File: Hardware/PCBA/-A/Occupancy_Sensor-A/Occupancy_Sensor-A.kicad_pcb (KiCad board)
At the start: 2 copper layers, 30 x 30 mm, 60 parts, among them J1 USB_C_Receptacle, J2 Conn_02x05_Odd_Even, Q1 2N7002, Q2 2N7002, SW1 SW_Push, SW2 SW_SPDT, U1 TPS78318DDCR, U3 TPS562200, U4 STM32WB55CGUx, U6 ECMF02-2AMX6, Y1 Crystal_GND24_Small, Y2 Crystal_GND24_Small

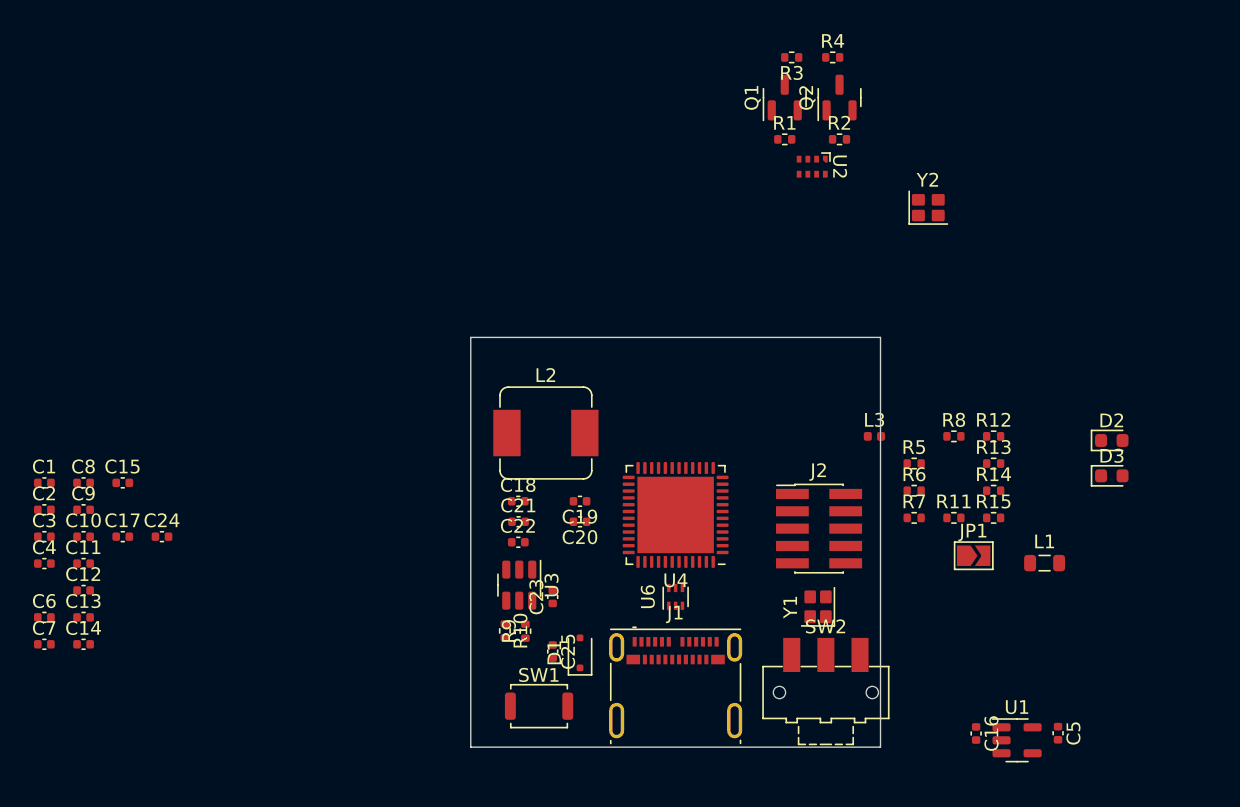
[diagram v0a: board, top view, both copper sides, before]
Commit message: General layout, regulator fixes
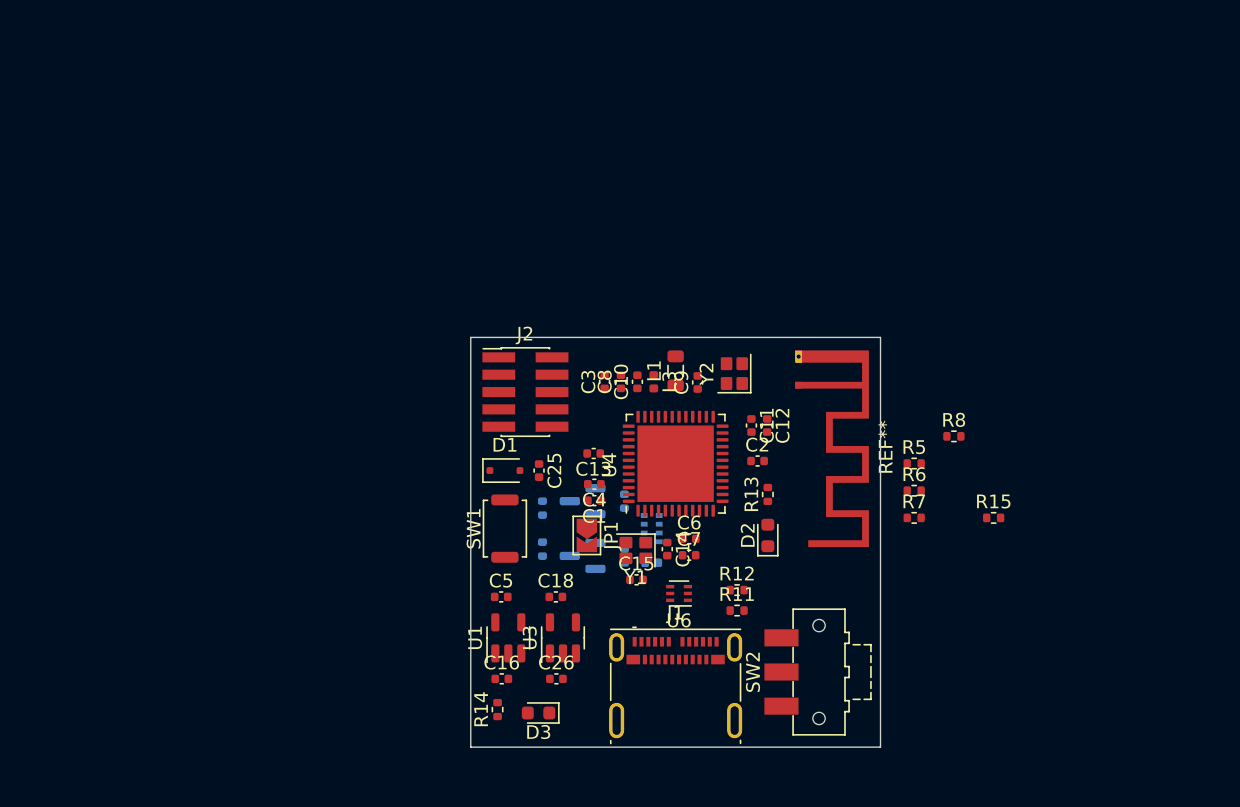
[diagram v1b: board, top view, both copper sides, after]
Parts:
- removed C19, C20: 22u, Capacitor_SMD:C_0402_1005Metric
- removed C21: 10u, Capacitor_SMD:C_0402_1005Metric
- removed C22, C23, C24: 100n, Capacitor_SMD:C_0402_1005Metric
- removed L2: 3.3u, Inductor_SMD:L_Sumida_CDMC6D28_7.25x6.5mm
- removed R10: 10K, Resistor_SMD:R_0402_1005Metric
- removed R9: 33.2K, Resistor_SMD:R_0402_1005Metric
- added C26: 1u, Capacitor_SMD:C_0402_1005Metric, F.Cu at (136.3, 125.0)
- added REF**: Texas_SWRA117D_2.4GHz_Right, RF_Antenna:Texas_SWRA117D_2.4GHz_Right, F.Cu at (154.0, 103.5)
- C17, Q1, Q2, R1, R2, R3, R4, U2: moved to B.Cu
- C18: value 10u -> 1u
- C5: value 2.2u -> 1u
- U1: value TPS78318DDCR -> TPS7A0333PDBV
- U3: value TPS562200 -> TPS7A03185PDBV; footprint Package_TO_SOT_SMD:SOT-23-6 -> Package_TO_SOT_SMD:SOT-23-5
- moved C2 52.3 mm to (151.0, 109.0)
- moved C12 51.5 mm to (151.7, 106.5), turned to -90 degrees
- moved C11 49.9 mm to (150.6, 106.5), turned to -90 degrees
- moved C7 47.7 mm to (146.0, 116.0)
- moved C6 47.6 mm to (146.0, 114.8)
- moved C9 45.9 mm to (146.6, 103.3), turned to 90 degrees
- moved D3 45.4 mm to (135.0, 127.5), turned to 180 degrees
- moved C14 43.3 mm to (144.4, 115.5), turned to -90 degrees
- moved C3 42.6 mm to (139.8, 103.2), turned to 90 degrees
- moved C10 42.1 mm to (142.2, 103.2), turned to 90 degrees
- moved C5 42.0 mm to (132.2, 119.0), turned to 0 degrees
- moved R4 41.8 mm to (135.2, 115.5), turned to -90 degrees
- moved C4 40.7 mm to (139.1, 110.8), turned to 180 degrees
- moved C1 40.3 mm to (139.1, 112.0), turned to 180 degrees
- moved C8 40.0 mm to (141.0, 103.2), turned to 90 degrees
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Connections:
- C15 pad 1: /OSC32_OUT -> /OSC32_IN
- C16 pad 1: +3.3V -> VBUS
- C18 pad 1: VBUS -> +1V8
- C5 pad 1: +1V8 -> +3.3V
- U1 pad 1: +3.3V -> VBUS
- U1 pad 3: 1V8_EN -> VBUS
- U1 pad 4: GND -> unconnected-(U1-NC-Pad4)
- U1 pad 5: +1V8 -> +3.3V
- U3 pad 1: GND -> VBUS
- U3 pad 2: Net-(U3-SW) -> GND
- U3 pad 3: VBUS -> 1V8_EN
- U3 pad 4: Net-(U3-VFB) -> unconnected-(U3-NC-Pad4)
- U3 pad 5: VBUS -> +1V8

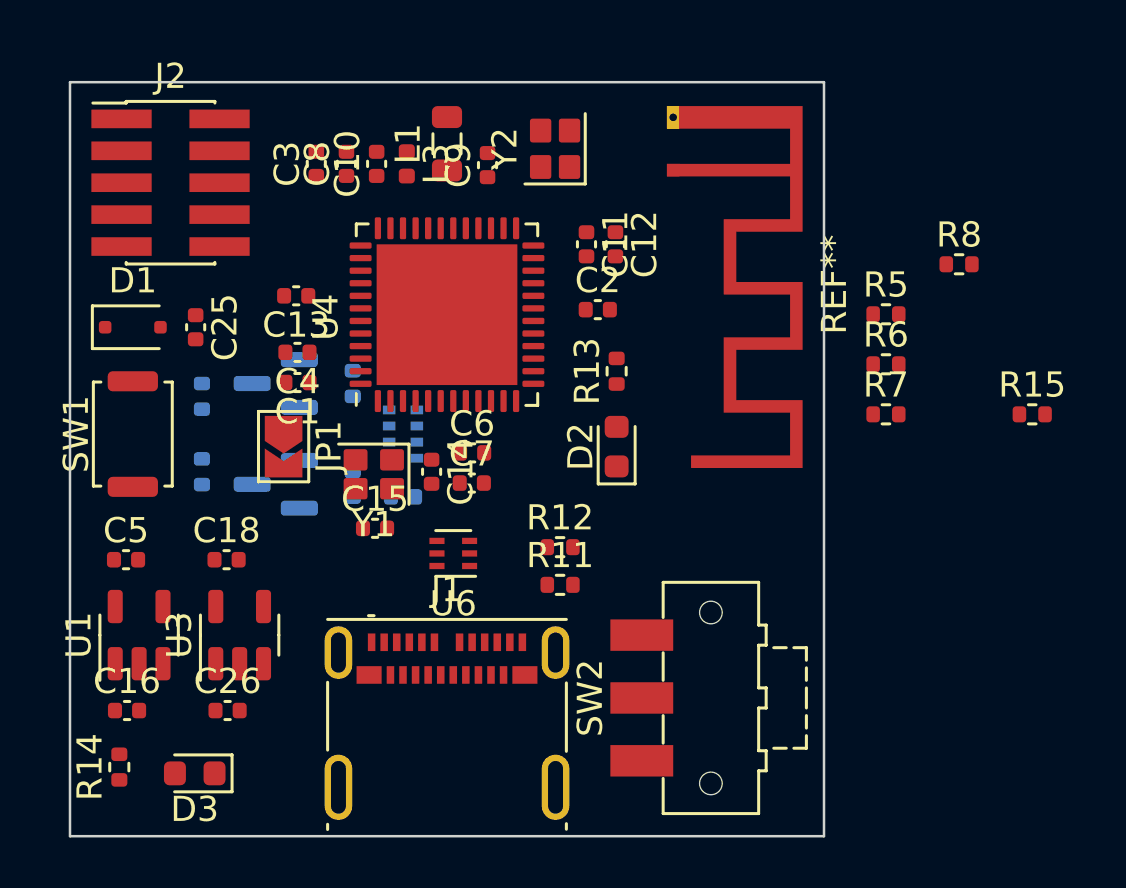
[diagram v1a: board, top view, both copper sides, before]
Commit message: Add TOF footprint, component to schematic
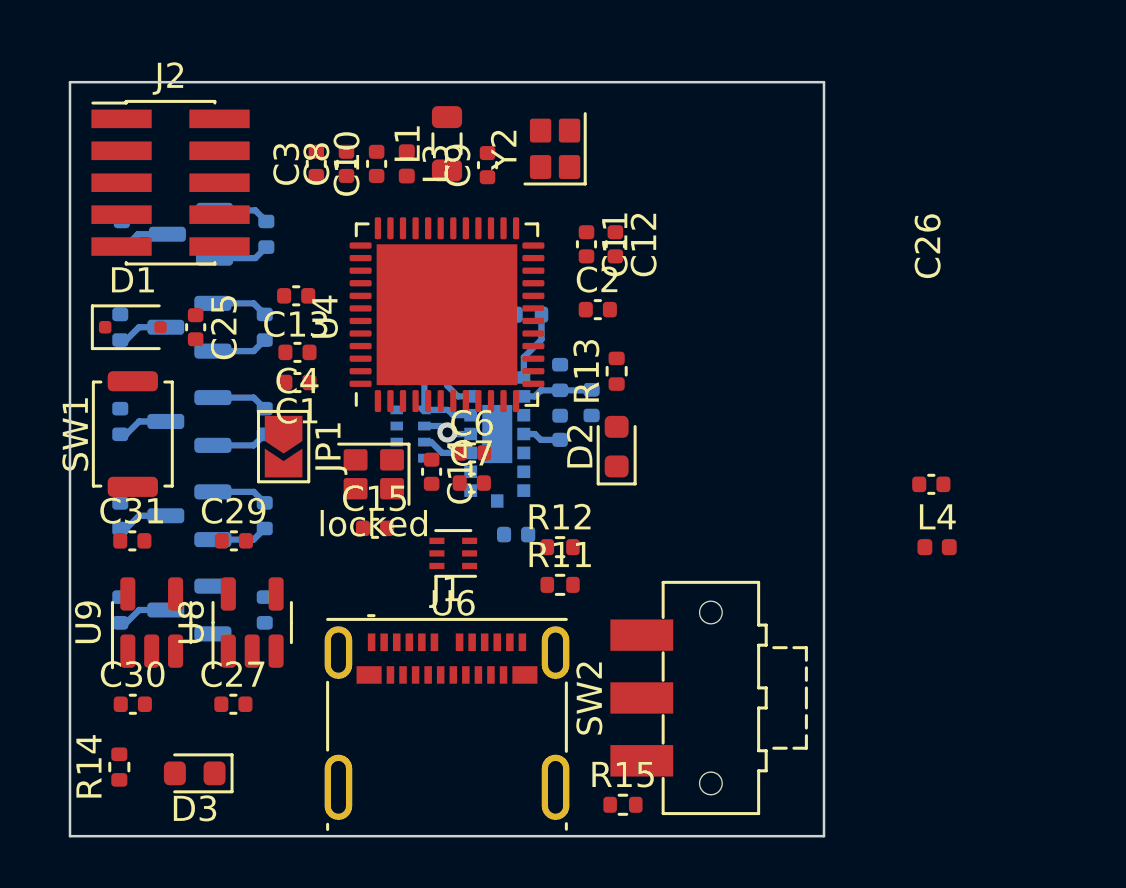
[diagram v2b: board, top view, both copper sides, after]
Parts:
- removed R1: 10K, Resistor_SMD:R_0402_1005Metric
- removed R5: 22R, Resistor_SMD:R_0402_1005Metric
- removed R6: 2.2K, Resistor_SMD:R_0402_1005Metric
- removed REF**: Texas_SWRA117D_2.4GHz_Right, RF_Antenna:Texas_SWRA117D_2.4GHz_Right
- removed U3: TPS7A03185PDBV, Package_TO_SOT_SMD:SOT-23-5
- added C27: 1u, Capacitor_SMD:C_0402_1005Metric, F.Cu at (136.5, 124.8)
- added C29: 1u, Capacitor_SMD:C_0402_1005Metric, F.Cu at (136.5, 118.2)
- added C30: 1u, Capacitor_SMD:C_0402_1005Metric, F.Cu at (132.5, 124.8)
- added C31: 1u, Capacitor_SMD:C_0402_1005Metric, F.Cu at (132.5, 118.2)
- added L4: L, Inductor_SMD:L_0402_1005Metric, F.Cu at (164.5, 118.5)
- added Q3: 2N7002, Package_TO_SOT_SMD:SOT-23, B.Cu at (134.8, 121.0)
- added Q4: 2N7002, Package_TO_SOT_SMD:SOT-23, B.Cu at (134.8, 109.8)
- added Q5: 2N7002, Package_TO_SOT_SMD:SOT-23, B.Cu at (134.8, 117.2)
- added R10: 40K, Resistor_SMD:R_0402_1005Metric, B.Cu at (149.5, 111.8)
- added R16: 47K, Resistor_SMD:R_0402_1005Metric, B.Cu at (137.8, 117.2)
- added R17: 47K, Resistor_SMD:R_0402_1005Metric, B.Cu at (132.0, 117.2)
- added R20: 2.2K, Resistor_SMD:R_0402_1005Metric, B.Cu at (137.8, 113.5)
- added R21: 2.2K, Resistor_SMD:R_0402_1005Metric, B.Cu at (132.0, 113.5)
- added R22: 2.2K, Resistor_SMD:R_0402_1005Metric, B.Cu at (137.8, 106.0)
- added R23: 2.2K, Resistor_SMD:R_0402_1005Metric, B.Cu at (132.1, 106.0)
- added R24: 2.2K, Resistor_SMD:R_0402_1005Metric, B.Cu at (137.8, 109.8)
- added R25: 2.2K, Resistor_SMD:R_0402_1005Metric, B.Cu at (132.0, 109.8)
- added R9: 47K, Resistor_SMD:R_0402_1005Metric, B.Cu at (150.8, 112.8)
- added U8: TPS7A03185PDQNR, Package_TO_SOT_SMD:SOT-23-5, F.Cu at (137.2, 121.5)
- added U9: TPS7A0333PDBVR, Package_TO_SOT_SMD:SOT-23-5, F.Cu at (133.2, 121.5)
- C16: value 1u -> 100n; moved to B.Cu
- C17: value 1u -> 100n
- C18: moved to B.Cu
- C26: value 1u -> C_Small
- C5: value 1u -> 4.7u; moved to B.Cu
- R2, R4: value 10K -> 47K
- R3: value 10K -> 40K
- R7, R8: value 2.2K -> 47K; moved to B.Cu
- U1: value TPS7A0333PDBV -> TCS3430; footprint Package_TO_SOT_SMD:SOT-23-5 -> Occupancy_Sensor_Custom_Footprints:TCS3430; moved to B.Cu
- U2: value ~ -> VL53L8CX; footprint Occupancy_Sensor_Custom_Footprints:TCS3430 -> Occupancy_Sensor_Custom_Footprints:VL53L8CX
- moved R8 36.1 mm to (132.0, 121.0), turned to -90 degrees
- moved C26 29.4 mm to (164.3, 116.0)
- moved R7 25.9 mm to (137.8, 121.0), turned to -90 degrees
- moved R15 22.5 mm to (152.0, 128.8)
- moved C16 18.4 mm to (143.6, 110.5), turned to 180 degrees
- moved C5 18.1 mm to (149.5, 113.8), turned to 90 degrees
- moved U1 13.4 mm to (143.6, 114.0), turned to 180 degrees
- moved R4 12.4 mm to (146.0, 109.2), turned to 0 degrees
- moved Q2 10.5 mm to (134.8, 106.0)
- moved C18 10.3 mm to (143.6, 111.8), turned to 180 degrees
- moved R2 9.72 mm to (148.2, 109.2), turned to 180 degrees
- moved R3 8.91 mm to (143.6, 109.2), turned to 0 degrees
- moved C17 4.74 mm to (147.8, 118.0)
- moved Q1 3.75 mm to (134.8, 113.5)
- moved U2 3.75 mm to (147.0, 114.0), turned to 90 degrees
- renumbered Y1 to locked
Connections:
- C15 pad 1: /OSC32_IN -> /OSC32_OUT
- C16 pad 1: VBUS -> +1V8
- C17 pad 1: Net-(U2-VDD) -> +1V8
- C26 pad 1: VBUS -> unconnected-(C26-Pad1)
- C26 pad 2: GND -> unconnected-(C26-Pad2)
- Q1 pad 2: /SCL_1V8 -> /INT_CLR_1V8
- Q1 pad 3: /SCL -> /INT_CLR
- Q2 pad 2: /SDA_1V8 -> /SCL_1V8
- Q2 pad 3: /SDA -> /SCL_3V3
- R2 pad 1: +1V8 -> Net-(U2-SPI_I2C_N)
- R2 pad 2: /SDA_1V8 -> GND
- R3 pad 1: +3V3 -> /LPn
- R3 pad 2: /SCL -> /LPn_1V8
- R4 pad 1: +3V3 -> /LPn_1V8
- R4 pad 2: /SDA -> GND
- R7 pad 2: /SCL_1V8 -> /SYNC_1V8
- R8 pad 1: +1V8 -> +3.3V
- R8 pad 2: Net-(U2-INT) -> /SYNC_3V3
- U1 pad 1: VBUS -> +1V8
- U1 pad 2: GND -> /SDA_1V8
- U1 pad 3: VBUS -> /SCL_1V8
- U1 pad 4: unconnected-(U1-NC-Pad4) -> /INT_CLR_1V8
- U1 pad 5: +3.3V -> unconnected-(U1-N/C-Pad5)
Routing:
- net +1V8: track 0.00 -> 13.3 mm
- net /LPn_1V8: track 0.00 -> 5.08 mm
- net /SDA_1V8: track 0.00 -> 4.28 mm, vias 0 -> 1
- net /SCL_1V8: track 0.00 -> 4.27 mm
- net /INT_TOF_1V8: track 0.00 -> 4.02 mm
- net /I2C_RST_1V8: track 0.00 -> 2.81 mm
- net Net-(U2-SPI_I2C_N): track 0.00 -> 2.79 mm
- net /INT_CLR_1V8: track 0.00 -> 2.24 mm
- net /SYNC_3V3: track 0.00 -> 2.02 mm
- net /SDA_3V3: track 0.00 -> 2.02 mm
- net /SCL_3V3: track 0.00 -> 2.02 mm
- net /INT_TOF: track 0.00 -> 2.02 mm
- net /INT_CLR: track 0.00 -> 2.02 mm
- net +3.3V: track 0.00 -> 1.54 mm
